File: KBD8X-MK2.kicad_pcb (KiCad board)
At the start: 2 copper layers, 343.7 x 118.3 mm, 347 parts, among them J1 AVR-ISP-6, Q1 DSS60601MZ4-13, SW1 SW_Push, SW2 SW_SPDT, SW3 SW_SPDT, U1 ATmega32U4-MU, U2 PRTR5V0U2X, Y1 16MHz

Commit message: Add warning text
Also delete and untrack backup files
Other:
- board text added: "KBD8X-MKII PCB Rev 2.0 20190404 ver. Noflex"
- board text added: "WARNING: THIS IS NOT AN ORIGINAL PCB. NOT MADE BY AI03 OR KBDFANS. NO WARRANTY."
- board text removed: "KBD8X-MKII PCB Rev 2.0 20190404"
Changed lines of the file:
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@@
-(kicad_pcb (version 20171130) (host pcbnew "(5.0.2)-1")
+(kicad_pcb (version 20171130) (host pcbnew "(5.1.5)-3")
   (general
     (thickness 1.6)
-    (drawings 75)
+    (drawings 76)
     (tracks 3915)
     (zones 0)
@@
     (zone_45_only no)
     (trace_min 0.2)
-    (segment_width 0.2)
-    (edge_width 0.2)
     (via_size 0.6)
     (via_drill 0.4)
@@
     (uvia_min_size 0.2)
     (uvia_min_drill 0.1)
+    (edge_width 0.2)
+    (segment_width 0.2)
     (pcb_text_width 0.3)
     (pcb_text_size 1.5 1.5)
@@
     (pad "" np_thru_hole circle (at 5.08 0 48.0996) (size 1.75 1.75) (drill 1.75) (layers *.Cu *.Mask))
   )
+  (gr_text "WARNING: THIS IS NOT AN ORIGINAL PCB.\nNOT MADE BY AI03 OR KBDFANS.\nNO WARRANTY." (at 238.125 52.3875) (layer B.SilkS)
+    (effects (font (size 1.5 1.5) (thickness 0.3)) (justify mirror))
+  )
   (gr_circle (center 238.125 146.685) (end 240.625 146.685) (layer Cmts.User) (width 0.2))
   (gr_text RESET (at 365.252 105.664 90) (layer B.SilkS)
@@
     (effects (font (size 1.5 1.5) (thickness 0.3)) (justify mirror))
   )
-  (gr_text "KBD8X-MKII PCB Rev 2.0 20190404" (at 90.4875 92.456) (layer B.SilkS)
+  (gr_text "KBD8X-MKII PCB Rev 2.0 20190404\nver. Noflex" (at 90.4875 92.456) (layer B.SilkS)
     (effects (font (size 1.5 1.5) (thickness 0.3)) (justify mirror))
   )

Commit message: Add top reset switch & more warning text
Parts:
- added SW4: SW_Push, random-keyboard-parts:SKQG-1155865, F.Cu at (206.4, 137.3)
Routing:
- net RESET: track 53.7 -> 236.5 mm, vias 0 -> 6
- net GND: track 1191.1 -> 1217.6 mm, vias 19 -> 20
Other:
- outline, holes or cut-outs redrawn
- board text added: "Produced under the terms of the Creative Commons Attribution-NonCommercial 4.0 International license"
- board text added: "https://github.com/gwerbin/KBD8X-MKII-PCB"

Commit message: Push some traces
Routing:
- net RESET: track 236.5 -> 239.5 mm, vias 6 -> 5
- net GND: track 1217.6 -> 1215.8 mm

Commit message: Modify text
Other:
- board text added: "KBD8X-MKII PCB ver. Noflex Rev 1.0 based on KBD8X-MKII PCB Rev 2.0 20190404"
- board text added: "Made to fit the"
- board text added: "THIS IS NOT AN ORIGINAL PCB. IT IS NOT MADE BY AI03 OR KBDFANS. THERE IS ABSOLUTELY NO WARRANTY. USE AT YOUR OWN RISK."
- board text removed: "KBD8X-MKII PCB Rev 2.0 20190404 ver. Noflex"
- board text removed: "WARNING: THIS IS NOT AN ORIGINAL PCB. NOT MADE BY AI03 OR KBDFANS. NO WARRANTY."
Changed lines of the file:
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@@
   (general
     (thickness 1.6)
-    (drawings 71)
+    (drawings 72)
     (tracks 3951)
     (zones 0)
@@
     (pad 4 smd rect (at -3.1 1.85 180) (size 1.8 1.1) (layers F.Cu F.Paste F.Mask))
   )
+  (gr_text "Made to fit the" (at 134.9375 133.35) (layer F.SilkS)
+    (effects (font (size 1.5 1.5) (thickness 0.3)))
+  )
   (gr_text RESET (at 201.422 137.287 90) (layer F.SilkS)
     (effects (font (size 1 1) (thickness 0.15)))
   )
-  (gr_text https://github.com/gwerbin/KBD8X-MKII-PCB (at 200.025 111.125) (layer B.SilkS)
+  (gr_text https://github.com/gwerbin/KBD8X-MKII-PCB (at 243.68125 92.86875) (layer B.SilkS)
     (effects (font (size 1.5 1.5) (thickness 0.3)) (justify mirror))
   )
-  (gr_text "Produced under the terms of the Creative Commons Attribution-NonCommercial 4.0 International license" (at 200.025 73.025) (layer B.SilkS)
-    (effects (font (size 1.5 1.5) (thickness 0.3)) (justify mirror))
+  (gr_text "Produced under the terms of the Creative Commons Attribution-NonCommercial 4.0 International license" (at 180.975 111.125) (layer B.SilkS)
+    (effects (font (size 1.5 1.5) (thickness 0.3) italic) (justify mirror))
   )
-  (gr_text "WARNING: THIS IS NOT AN ORIGINAL PCB.\nNOT MADE BY AI03 OR KBDFANS.\nNO WARRANTY." (at 276.225 52.3875) (layer B.SilkS)
+  (gr_text "THIS IS NOT AN ORIGINAL PCB. IT IS NOT MADE BY AI03 OR KBDFANS.\nTHERE IS ABSOLUTELY NO WARRANTY. USE AT YOUR OWN RISK." (at 180.975 53.18125) (layer B.SilkS)
     (effects (font (size 1.5 1.5) (thickness 0.3)) (justify mirror))
   )
@@
     (effects (font (size 1.5 1.5) (thickness 0.3)) (justify mirror))
   )
-  (gr_text "KBD8X-MKII PCB Rev 2.0 20190404\nver. Noflex" (at 90.4875 92.456) (layer B.SilkS)
+  (gr_text "KBD8X-MKII PCB ver. Noflex Rev 1.0\nbased on KBD8X-MKII PCB Rev 2.0 20190404\n" (at 93.6625 92.456) (layer B.SilkS)
     (effects (font (size 1.5 1.5) (thickness 0.3)) (justify mirror))
   )

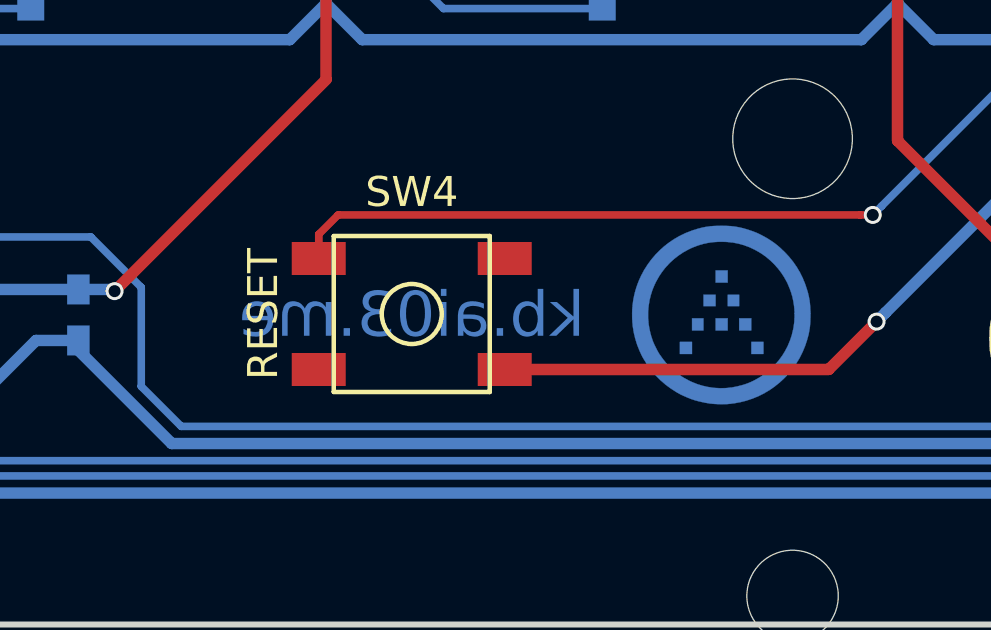
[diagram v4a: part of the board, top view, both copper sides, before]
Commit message: Tweak text, add ai03 aphorism
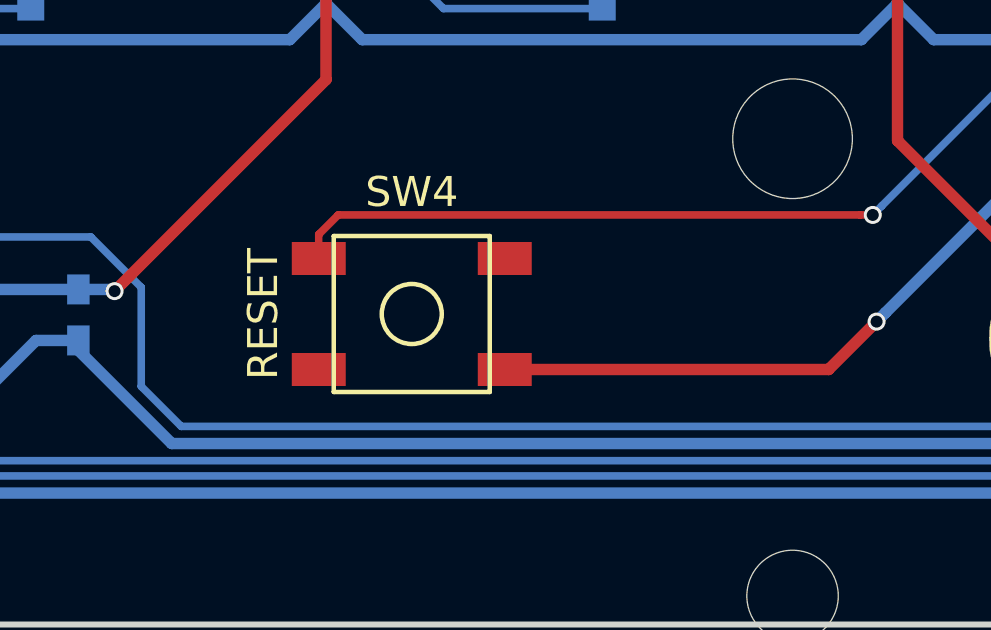
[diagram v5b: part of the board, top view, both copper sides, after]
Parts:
- removed the G*** at (216.7, 137.3) (x2)
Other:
- board text added: ""Anything is fine" -ai03"
- board text removed: "kb.ai03.me"
